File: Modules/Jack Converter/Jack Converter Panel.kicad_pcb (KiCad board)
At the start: 2 copper layers, 50 x 200 mm, 38 parts

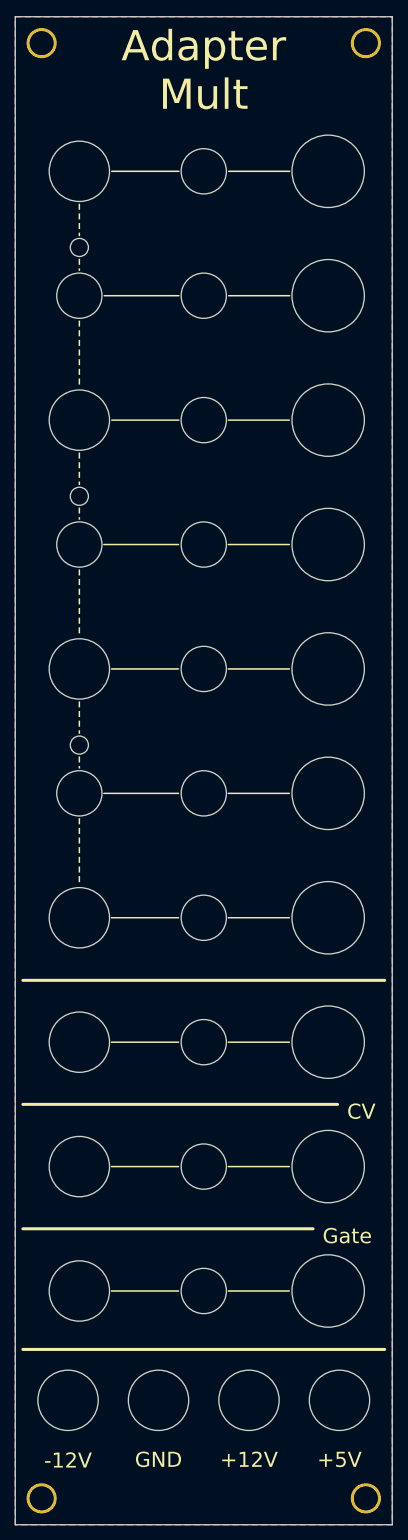
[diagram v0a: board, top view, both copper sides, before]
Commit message: Changed font to nullshock
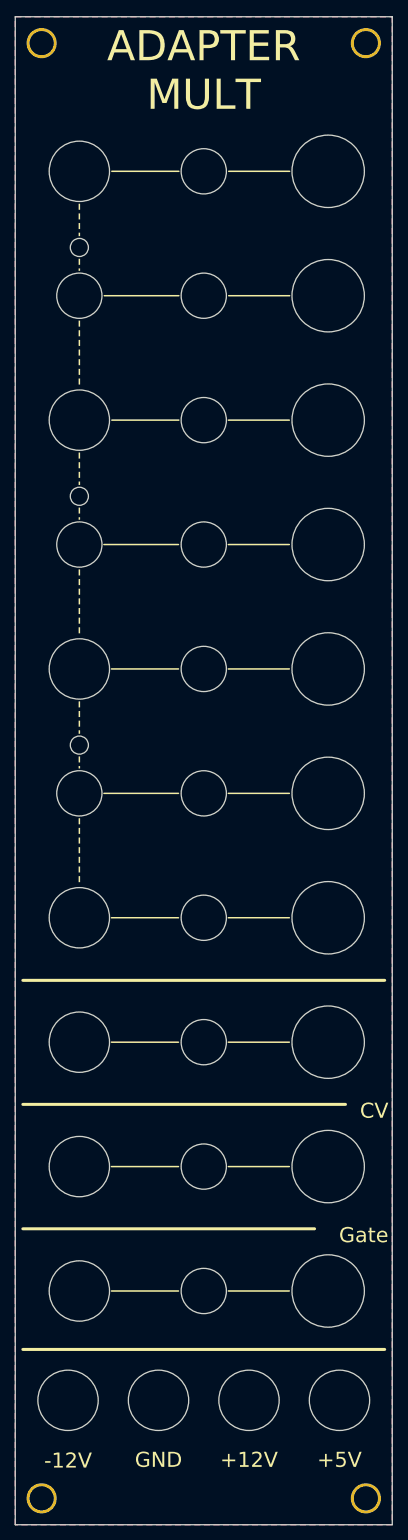
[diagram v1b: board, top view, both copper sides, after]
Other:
- board text added: "ADAPTER MULT"
- board text removed: "Adapter Mult"

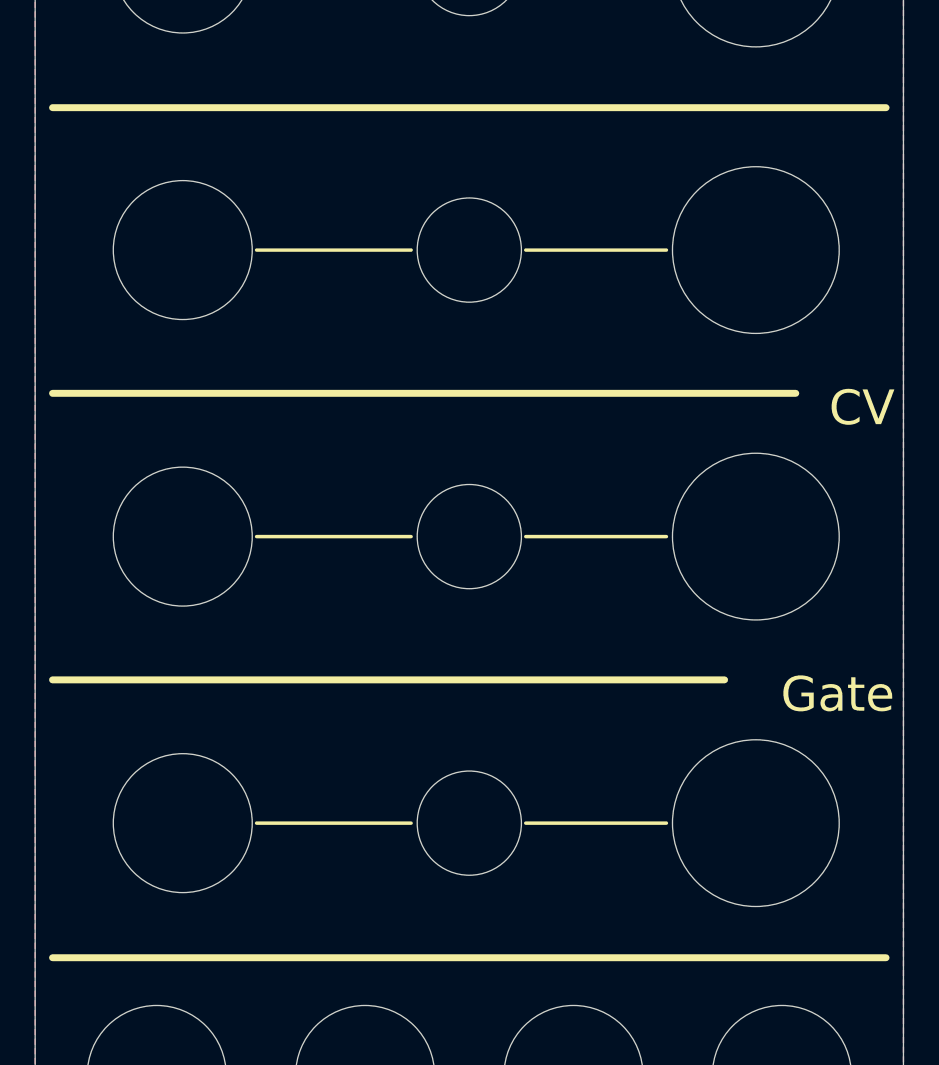
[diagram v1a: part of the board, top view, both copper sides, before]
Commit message: Made buffered mult panel
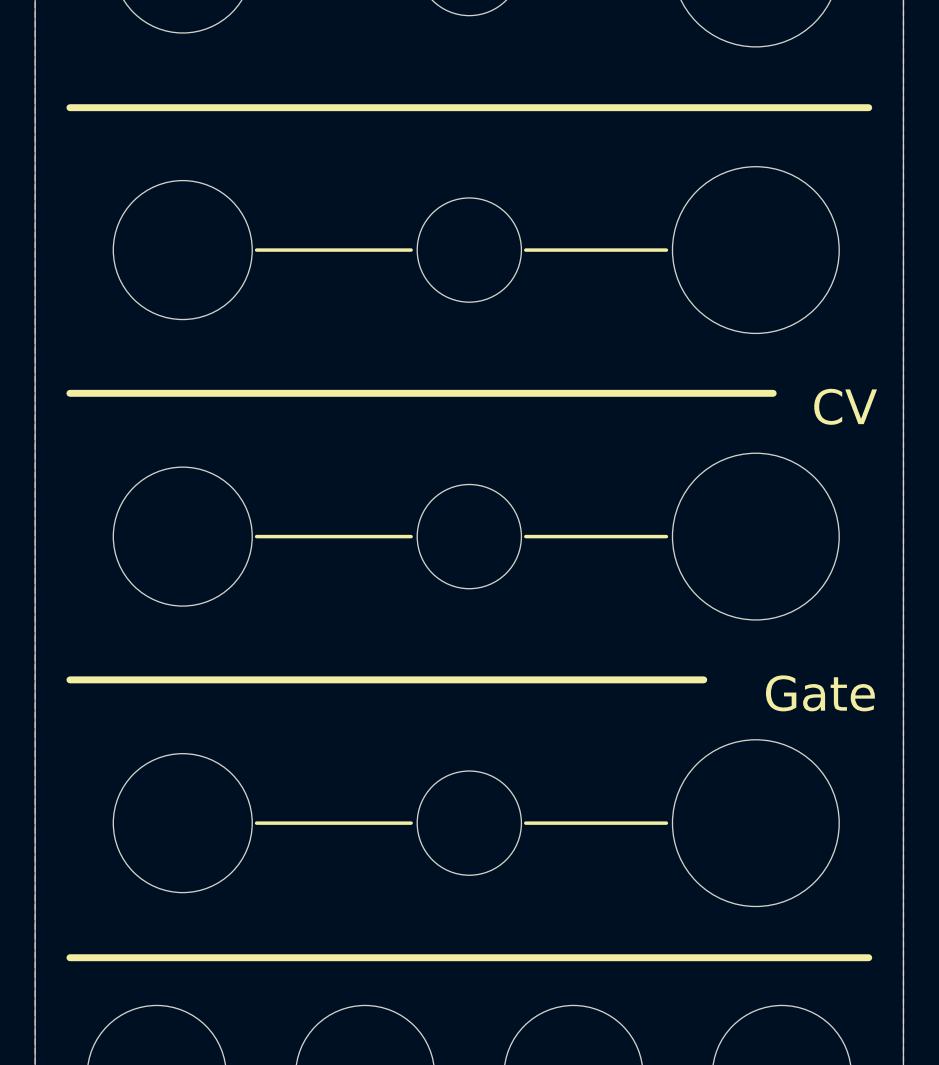
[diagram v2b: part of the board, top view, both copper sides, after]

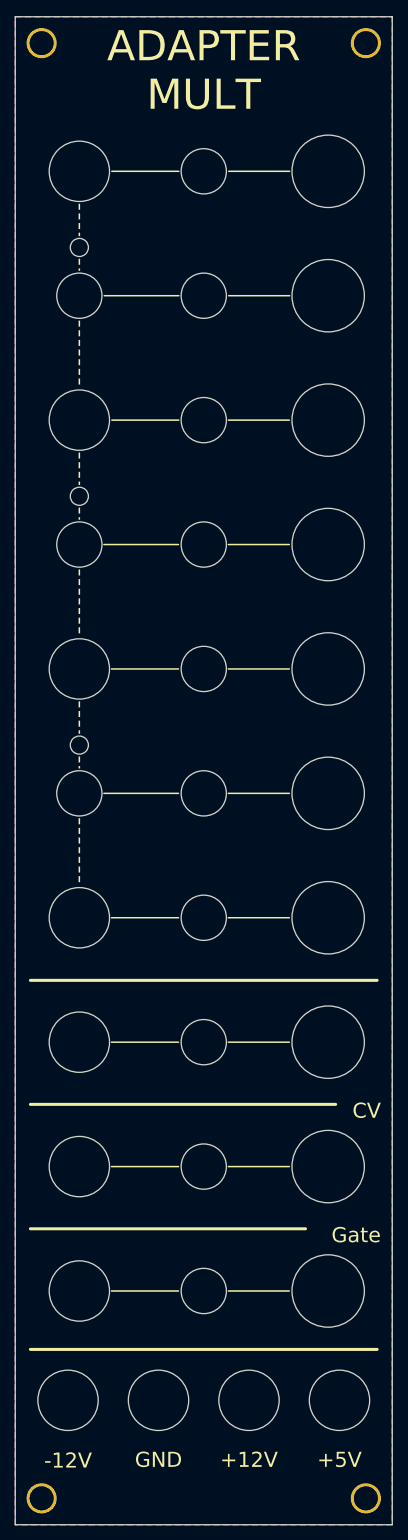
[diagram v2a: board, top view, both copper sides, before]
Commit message: Replaced holes with the latest fp version
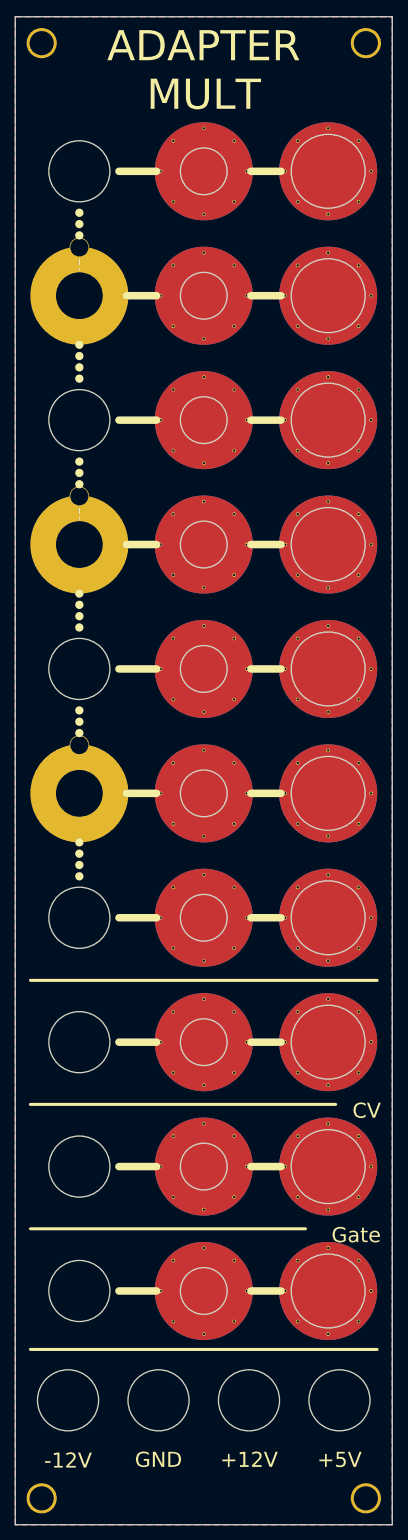
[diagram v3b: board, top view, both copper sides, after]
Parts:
- H10, H13, H16, H19, H22, H25, H28, H31, H34, H7: footprint SynthStuff:Jack_3.5mm_Cutout -> SynthStuff:Jack_3.5mm_Cutout_v2
- H11, H14, H17, H20, H23, H26, H29, H32, H35, H8: footprint SynthStuff:Jack_6.35mm_Cutout -> SynthStuff:Jack_6.35mm_Cutout_v2
- H12, H18, H24, H27, H30, H33, H36, H37, H38, H39, H6: footprint SynthStuff:Banana_Jack_Cutout -> SynthStuff:Banana_Jack_Cutout_v2

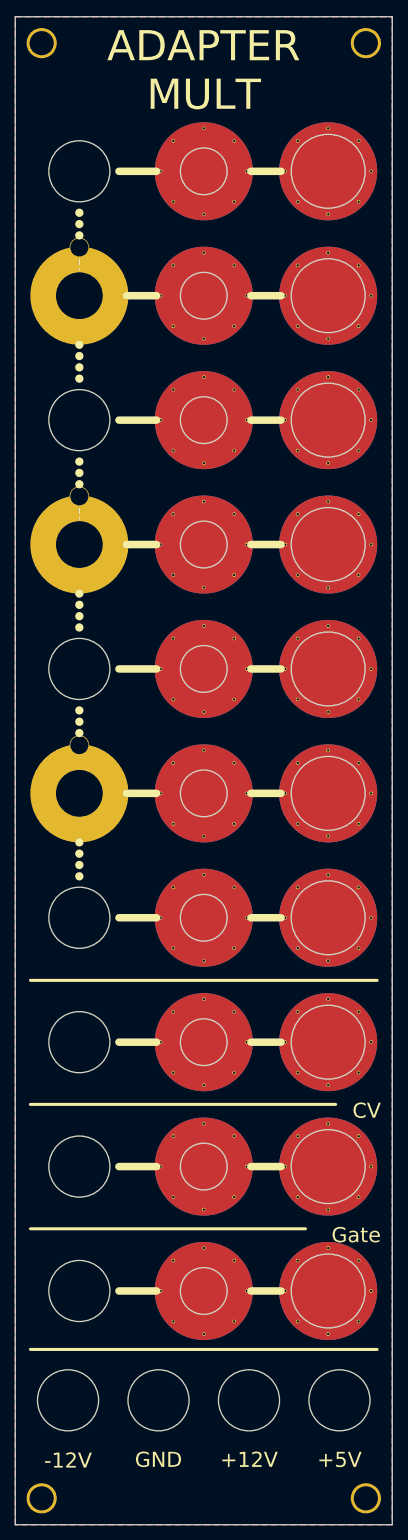
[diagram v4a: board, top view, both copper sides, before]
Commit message: Updated jack footprints to 12mm washer
... and added hash art to Adapter Mult CV and Gate jacks
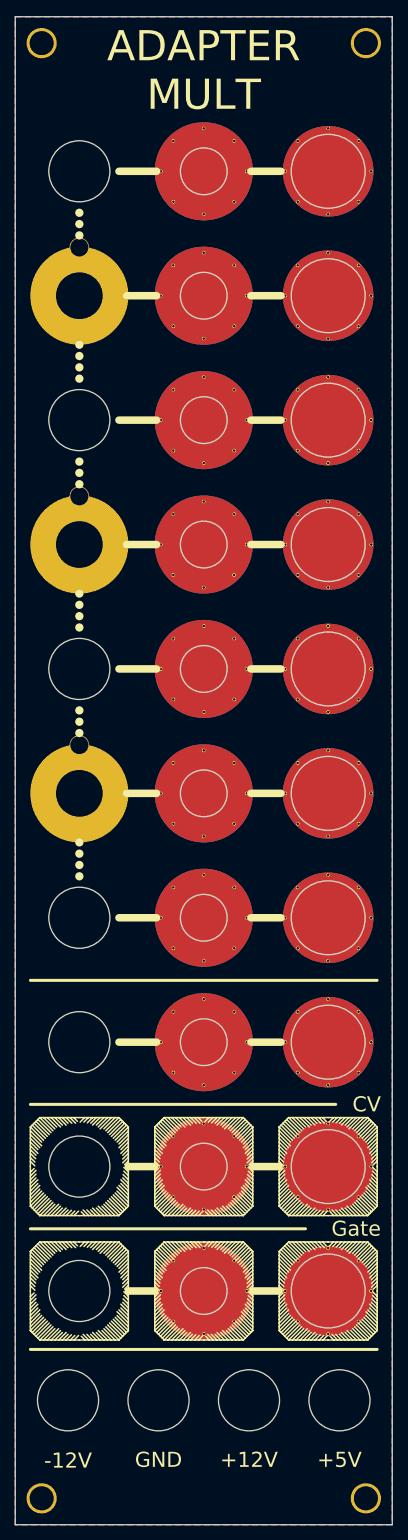
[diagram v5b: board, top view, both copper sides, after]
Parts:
- H1, H2, H3, H4: footprint SynthStuff:MountingHole_3.2mm_M3_Pad4mm -> SynthStuff:MountingHole_Rails
- H11, H14, H17, H20, H23, H26, H29, H32, H35, H8: footprint SynthStuff:Jack_6.35mm_Cutout_v2 -> SynthStuff:Jack_6.35mm_Cutout_v3
